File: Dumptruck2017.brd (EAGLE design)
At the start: 23.8 x 53.3 mm, 11 parts, among them IC1 317EMP

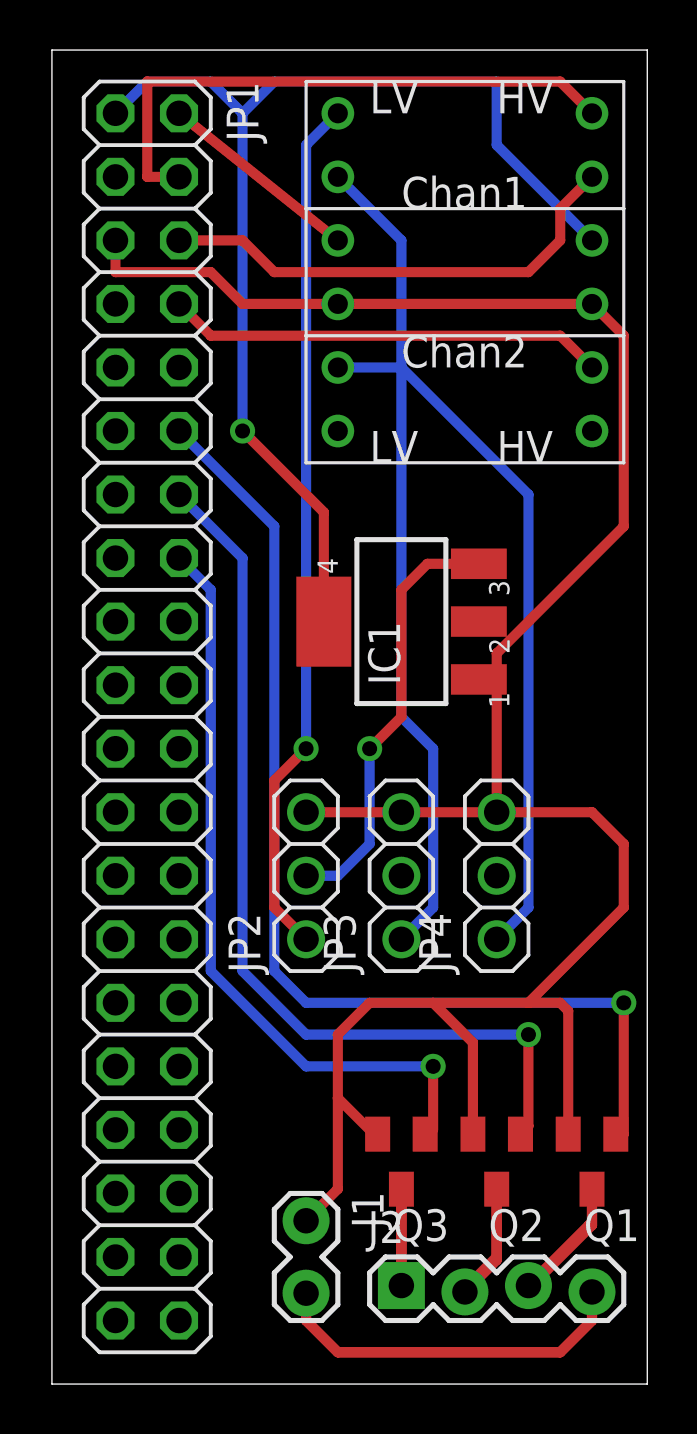
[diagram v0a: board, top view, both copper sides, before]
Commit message: made final changes to shrink board a bit and ordered this version
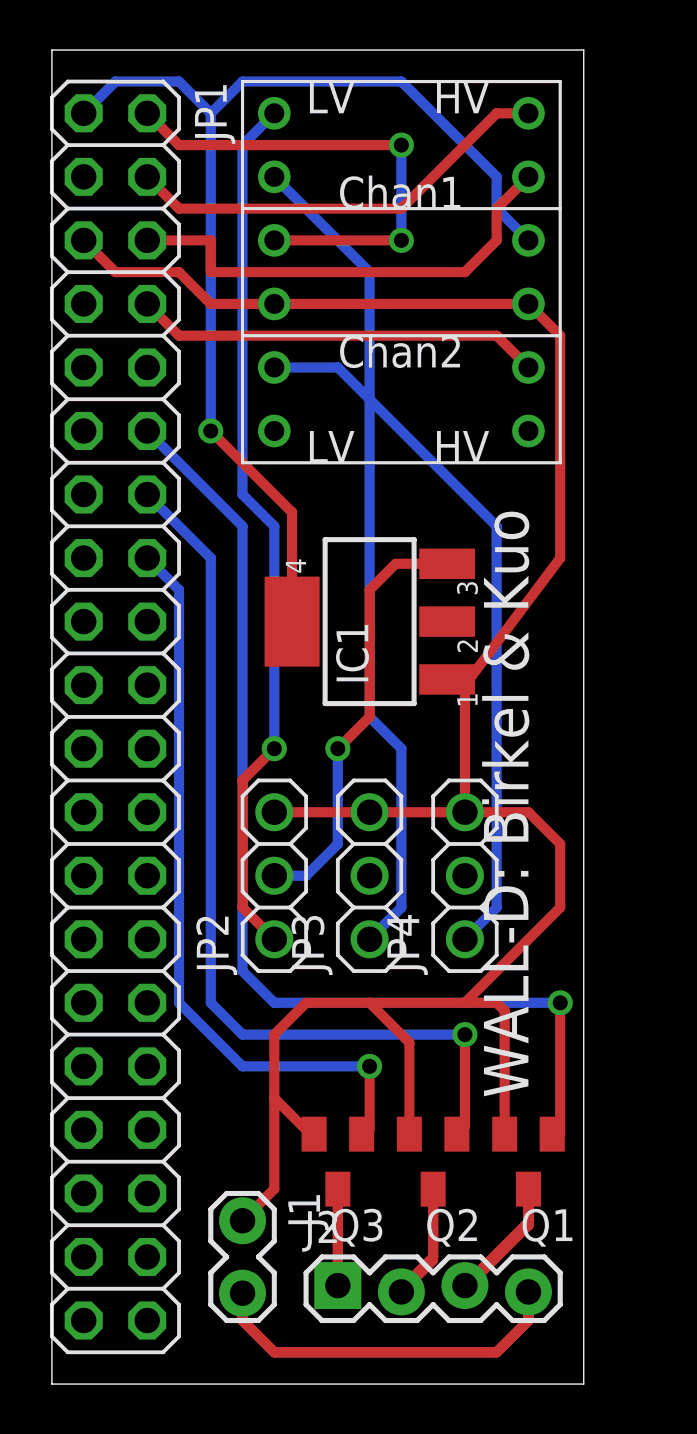
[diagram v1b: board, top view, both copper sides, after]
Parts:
- moved J2 2.54 mm to (11.4, 3.81)
- moved Q2 2.54 mm to (15.2, 8.89)
- moved Q3 2.54 mm to (11.4, 8.89)
- moved J1 2.54 mm to (7.62, 6.35)
- moved U$1 2.54 mm to (7.62, 36.8)
- moved Q1 2.54 mm to (19.1, 8.89)
- moved IC1 1.27 mm to (12.7, 30.5)
- moved JP3 1.27 mm to (12.7, 20.3)
- moved JP1 1.27 mm to (2.54, 26.7)
- moved JP2 1.27 mm to (8.89, 20.3)
- moved JP4 1.27 mm to (16.5, 20.3)
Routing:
- net +3V3: track 8.13 -> 19.6 mm, vias 0 -> 2
- net L_MTR_L: track 23.4 -> 17.3 mm
- net GND: track 96.5 -> 92.6 mm
- net +5V: track 46.4 -> 44.4 mm
- net ARM_MTR_L: track 17.6 -> 16.3 mm
- net LED1_SIG: track 43.2 -> 42.0 mm
- net LED3_SIG: track 30.0 -> 29.5 mm
- net R_MTR_L: track 19.4 -> 18.8 mm
- net R_MTR_H: track 32.6 -> 33.1 mm
- net LED2_SIG: track 36.7 -> 36.2 mm
- net ARM_MTR_H: track 28.0 -> 28.6 mm
- net L_MTR_H: track 34.6 -> 35.1 mm
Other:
- board size 23.8 x 53.3 mm -> 21.3 x 53.3 mm
- board text added: "WALL-D: Birkel & Kuo"
